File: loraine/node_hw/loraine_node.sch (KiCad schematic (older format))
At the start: 43 parts, among them CON1 BARREL_JACK, IC1 ATTINY2313A-S, P1 MOLEX, P2 MOLEX, P3 SOLDER_PAD, P4 ICSP, P5 OUTPUTS, P6 BUS, P7 BUS_THRU, Q1 BD679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

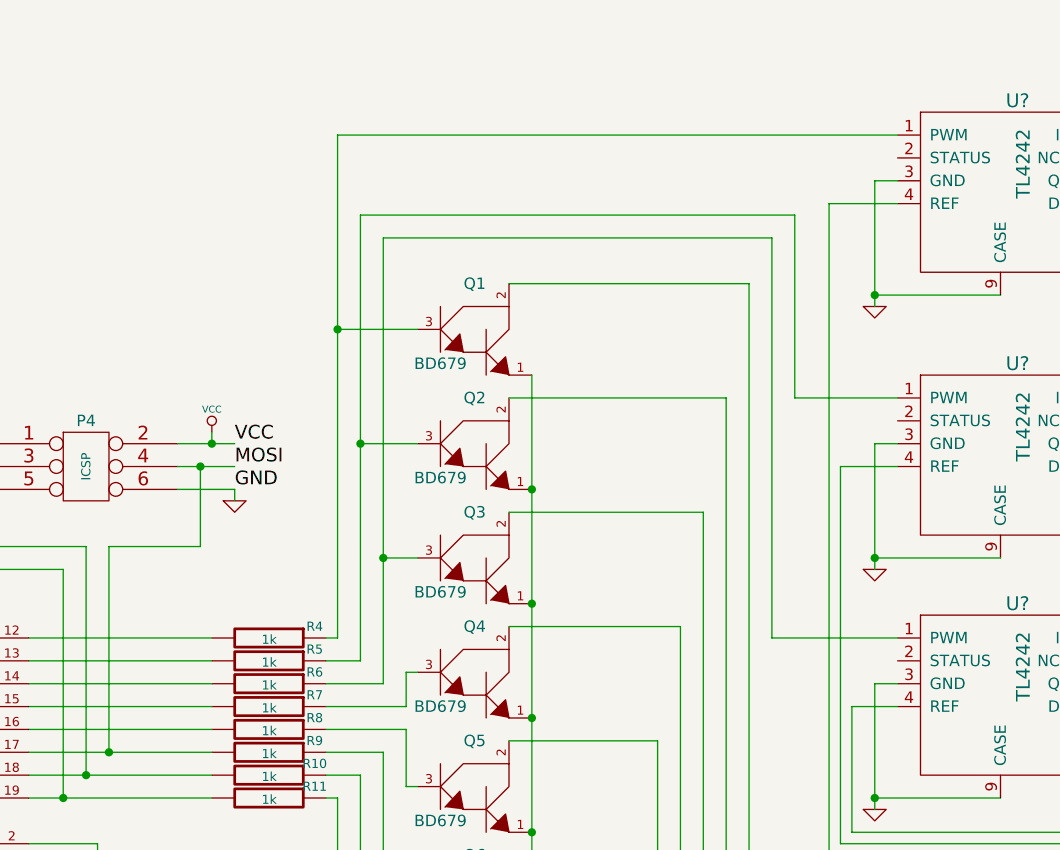
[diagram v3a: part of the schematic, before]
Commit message: Moved driver PWM conns to before BJT base resistors.
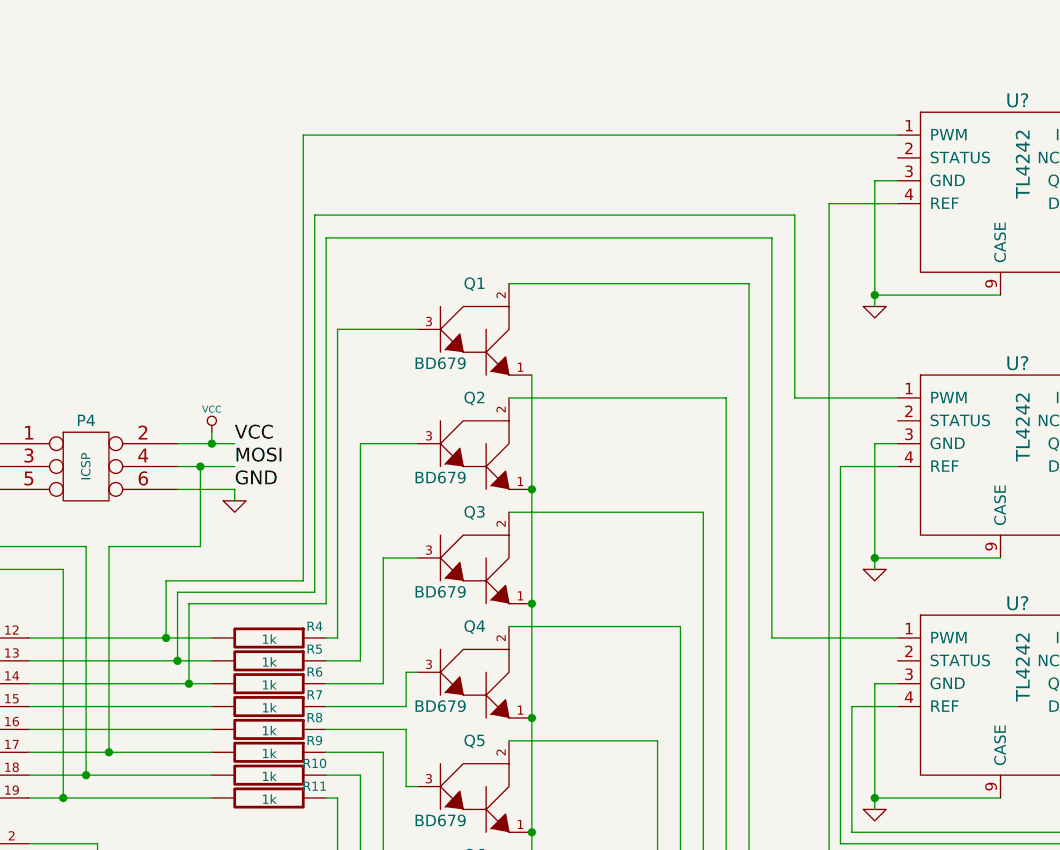
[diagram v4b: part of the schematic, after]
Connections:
- net at IC1.12 ((PCINT0/AIN0)PB0), R4.2: now also U?.1 (PWM)
- net at IC1.13 ((PCINT1/AIN1)PB1), R5.2: now also U?.1 (PWM)
- net at IC1.14 ((PCINT2/OC0A)PB2), R6.2: now also U?.1 (PWM)
- net at Q1.3, R4.1: no longer U?.1 (PWM)
- net at Q2.3, R5.1: no longer U?.1 (PWM)
- net at Q3.3, R6.1: no longer U?.1 (PWM)
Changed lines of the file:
@@
 	6150 3650 6100 3650
 Wire Wire Line
-	6150 1450 6150 3650
-Wire Wire Line
 	6250 3750 6100 3750
 Wire Wire Line
-	6250 1800 6250 3750
-Wire Wire Line
 	6250 2800 6500 2800
 Wire Wire Line
 	6350 3850 6100 3850
-Wire Wire Line
-	6350 1900 6350 3850
 Wire Wire Line
 	6350 3300 6500 3300
@@
 Connection ~ 8500 4350
 Wire Wire Line
-	6350 1900 8050 1900
+	6100 1900 8050 1900
 Wire Wire Line
 	8050 1900 8050 3650
 Wire Wire Line
 	8050 3650 8600 3650
-Connection ~ 6350 3300
-Wire Wire Line
-	6250 1800 8150 1800
+Wire Wire Line
+	6050 1800 8150 1800
 Wire Wire Line
 	8150 1800 8150 2600
 Wire Wire Line
 	8150 2600 8600 2600
-Connection ~ 6250 2800
-Wire Wire Line
-	6150 1450 8600 1450
-Connection ~ 6150 2300
+Wire Wire Line
+	6000 1450 8600 1450
 $Comp
 L R R?
@@
 Wire Wire Line
 	9600 3650 9600 3500
+Wire Wire Line
+	6150 2300 6150 3650
+Wire Wire Line
+	6250 2800 6250 3750
+Wire Wire Line
+	6350 3300 6350 3850
+Wire Wire Line
+	5500 3850 5500 3500
+Wire Wire Line
+	5500 3500 6100 3500
+Wire Wire Line
+	6100 3500 6100 1900
+Connection ~ 5500 3850
+Wire Wire Line
+	5450 3750 5450 3450
+Wire Wire Line
+	5450 3450 6050 3450
+Wire Wire Line
+	6050 3450 6050 1800
+Connection ~ 5450 3750
+Wire Wire Line
+	5400 3650 5400 3400
+Wire Wire Line
+	5400 3400 6000 3400
+Wire Wire Line
+	6000 3400 6000 1450
+Connection ~ 5400 3650
 $EndSCHEMATC

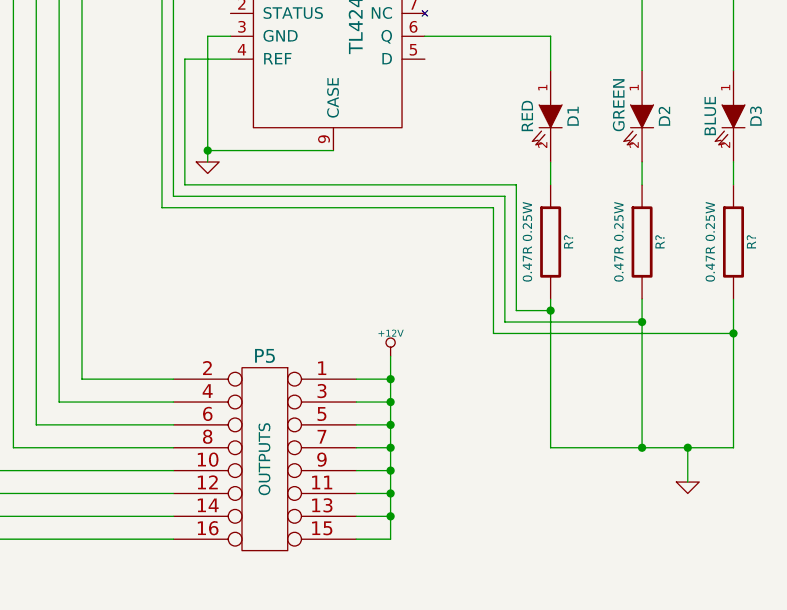
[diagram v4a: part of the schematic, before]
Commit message: Fixed driver current sense lines
TL4242 current sense lines went to ground instead of top of current sense resistors.
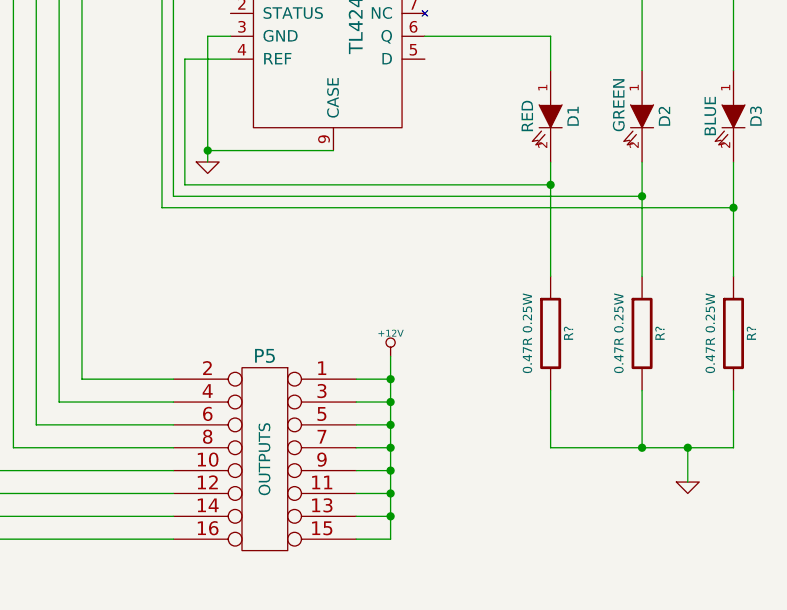
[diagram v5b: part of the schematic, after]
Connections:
- net GND: no longer U?.4 (REF), U?.4 (REF), U?.4 (REF)
- net at D1.2 (K), R?.1: now also U?.4 (REF)
- net at D2.2 (K), R?.1: now also U?.4 (REF)
- net at D3.2 (K), R?.1: now also U?.4 (REF)
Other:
- moved on the sheet: R?
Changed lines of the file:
@@
 $EndComp
-Wire Wire Line
-	10000 5000 10000 5650
 Wire Wire Line
 	10000 5650 10800 5650
-Wire Wire Line
-	10800 5650 10800 5000
-Wire Wire Line
-	10400 5000 10400 5650
 Connection ~ 10400 5650
 Wire Wire Line
@@
 L R R?
 U 1 1 5339FA1A
-P 10000 4750
-F 0 "R?" V 10080 4750 40  0000 C CNN
-F 1 "0.47R 0.25W" V 9900 4750 40  0000 C CNN
-F 2 "" V 9930 4750 30  0000 C CNN
-F 3 "" H 10000 4750 30  0000 C CNN
-	1    10000 4750
+P 10000 5150
+F 0 "R?" V 10080 5150 40  0000 C CNN
+F 1 "0.47R 0.25W" V 9900 5150 40  0000 C CNN
+F 2 "" V 9930 5150 30  0000 C CNN
+F 3 "" H 10000 5150 30  0000 C CNN
+	1    10000 5150
 	1    0    0    -1
 $EndComp
@@
 L R R?
 U 1 1 5339FA2E
-P 10400 4750
-F 0 "R?" V 10480 4750 40  0000 C CNN
-F 1 "0.47R 0.25W" V 10300 4750 40  0000 C CNN
-F 2 "" V 10330 4750 30  0000 C CNN
-F 3 "" H 10400 4750 30  0000 C CNN
-	1    10400 4750
+P 10400 5150
+F 0 "R?" V 10480 5150 40  0000 C CNN
+F 1 "0.47R 0.25W" V 10300 5150 40  0000 C CNN
+F 2 "" V 10330 5150 30  0000 C CNN
+F 3 "" H 10400 5150 30  0000 C CNN
+	1    10400 5150
 	1    0    0    -1
 $EndComp
@@
 L R R?
 U 1 1 5339FA42
-P 10800 4750
-F 0 "R?" V 10880 4750 40  0000 C CNN
-F 1 "0.47R 0.25W" V 10700 4750 40  0000 C CNN
-F 2 "" V 10730 4750 30  0000 C CNN
-F 3 "" H 10800 4750 30  0000 C CNN
-	1    10800 4750
-	1    0    0    -1
-$EndComp
-Wire Wire Line
-	10800 4500 10800 4400
-Wire Wire Line
-	10400 4400 10400 4500
-Wire Wire Line
-	10000 4500 10000 4400
+P 10800 5150
+F 0 "R?" V 10880 5150 40  0000 C CNN
+F 1 "0.47R 0.25W" V 10700 5150 40  0000 C CNN
+F 2 "" V 10730 5150 30  0000 C CNN
+F 3 "" H 10800 5150 30  0000 C CNN
+	1    10800 5150
+	1    0    0    -1
+$EndComp
 Wire Wire Line
 	10000 3850 10000 4000
@@
 	8400 3950 8400 4500
 Wire Wire Line
-	8400 4500 9850 4500
-Wire Wire Line
-	9850 4500 9850 5050
-Wire Wire Line
-	9850 5050 10000 5050
-Connection ~ 10000 5050
+	8400 4500 10000 4500
 Wire Wire Line
 	8600 2900 8350 2900
@@
 	8350 2900 8350 4550
 Wire Wire Line
-	8350 4550 9800 4550
-Wire Wire Line
-	9800 4550 9800 5100
-Wire Wire Line
-	9800 5100 10400 5100
-Connection ~ 10400 5100
+	8350 4550 10400 4550
 Wire Wire Line
 	8600 1750 8300 1750
@@
 	8300 1750 8300 4600
 Wire Wire Line
-	8300 4600 9750 4600
-Wire Wire Line
-	9750 4600 9750 5150
-Wire Wire Line
-	9750 5150 10800 5150
-Connection ~ 10800 5150
+	8300 4600 10800 4600
 Wire Wire Line
 	6900 5600 7250 5600
@@
 	6000 3400 6000 1450
 Connection ~ 5400 3650
+Connection ~ 10400 4550
+Connection ~ 10000 4500
+Connection ~ 10800 4600
+Wire Wire Line
+	10000 4400 10000 4900
+Wire Wire Line
+	10400 4400 10400 4900
+Wire Wire Line
+	10800 4400 10800 4900
+Wire Wire Line
+	10000 5400 10000 5650
+Wire Wire Line
+	10400 5400 10400 5650
+Wire Wire Line
+	10800 5650 10800 5400
 $EndSCHEMATC

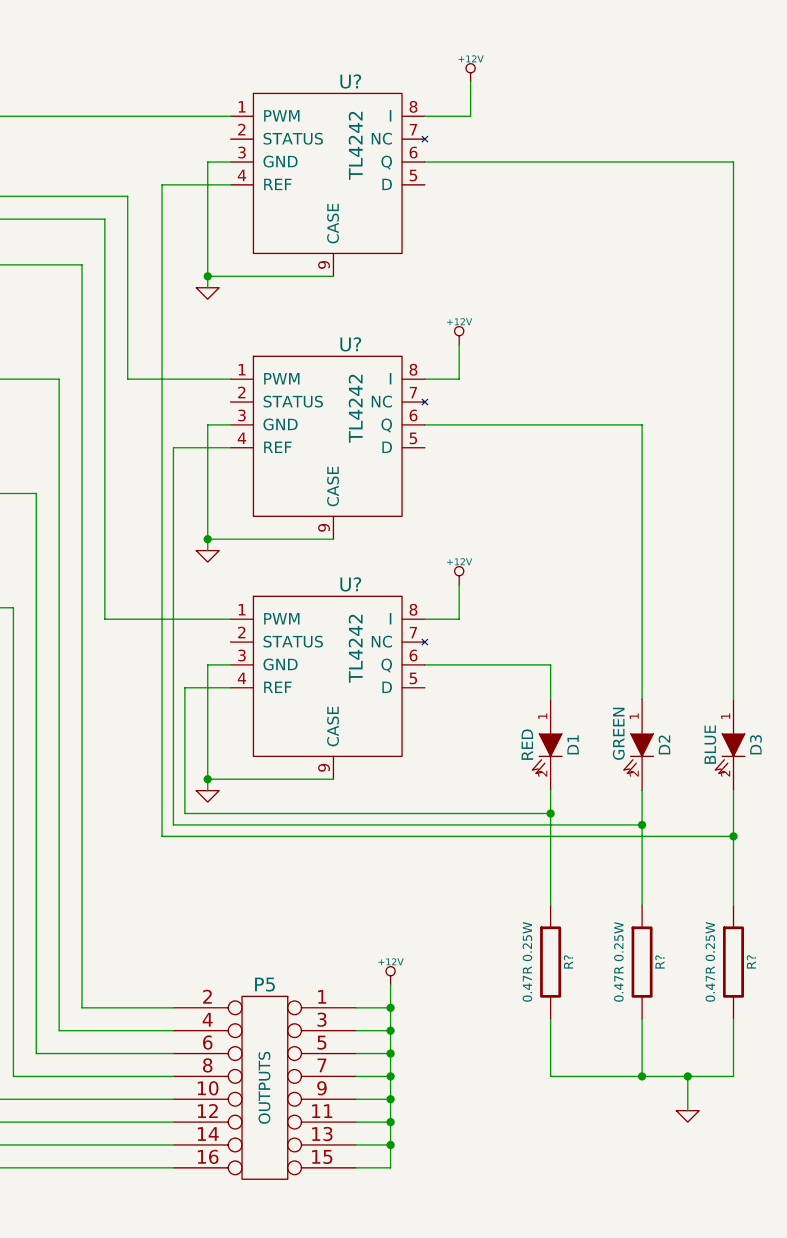
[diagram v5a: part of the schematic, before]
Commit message: Added star_led schematic component
Made new library star_led.lib with schematic component for RGB star LED with pinout matching Farnell 1716741.  Footprint to follow.
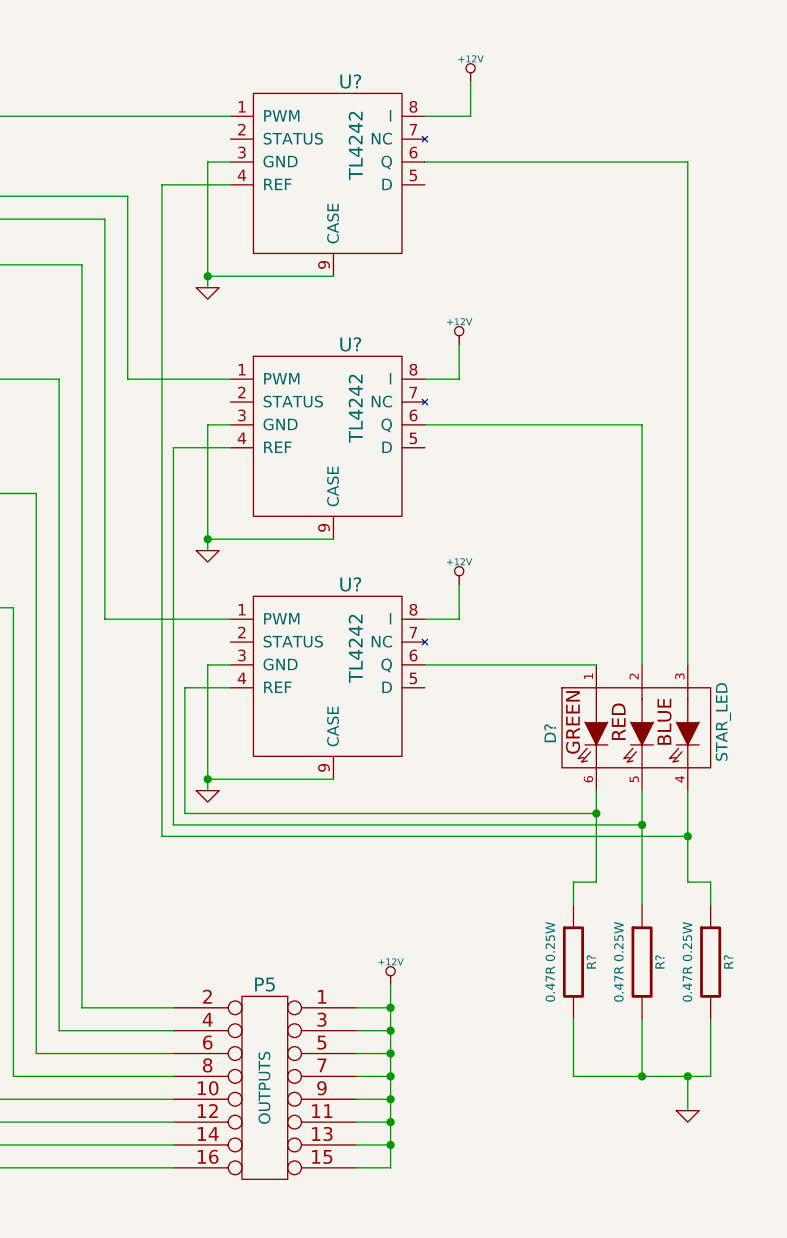
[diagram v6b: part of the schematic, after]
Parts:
- removed D1: RED, symbol LED
- removed D2: GREEN, symbol LED
- removed D3: BLUE, symbol LED
- added D?: STAR_LED, symbol STAR_LED
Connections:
- net at U?.6 (Q): now also D?.1 (G+)
- net at R?.1, U?.4 (REF): now also D?.6 (G-)
- net at U?.6 (Q): now also D?.2 (R+)
- net at R?.1, U?.4 (REF): now also D?.5 (R-)
- net at U?.6 (Q): now also D?.3 (B+)
- net at R?.1, U?.4 (REF): now also D?.4 (B-)
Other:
- moved on the sheet: R?
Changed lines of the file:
@@
 LIBS:bd679
 LIBS:tl4242
+LIBS:star_led
 LIBS:loraine_node-cache
 EELAYER 24 0
@@
 $EndComp
 $Comp
-L LED D1
-U 1 1 53389F99
-P 10000 4200
-F 0 "D1" H 10000 4300 50  0000 C CNN
-F 1 "RED" H 10000 4100 50  0000 C CNN
-F 2 "" H 10000 4200 60  0000 C CNN
-F 3 "" H 10000 4200 60  0000 C CNN
-	1    10000 4200
-	0    1    1    0
-$EndComp
-$Comp
-L LED D2
-U 1 1 53389FAD
-P 10400 4200
-F 0 "D2" H 10400 4300 50  0000 C CNN
-F 1 "GREEN" H 10350 4100 50  0000 C CNN
-F 2 "" H 10400 4200 60  0000 C CNN
-F 3 "" H 10400 4200 60  0000 C CNN
-	1    10400 4200
-	0    1    1    0
-$EndComp
-$Comp
-L LED D3
-U 1 1 53389FC1
-P 10800 4200
-F 0 "D3" H 10800 4300 50  0000 C CNN
-F 1 "BLUE" H 10800 4100 50  0000 C CNN
-F 2 "" H 10800 4200 60  0000 C CNN
-F 3 "" H 10800 4200 60  0000 C CNN
-	1    10800 4200
-	0    1    1    0
-$EndComp
-$Comp
 L C C6
 U 1 1 5338A896
@@
 	1    0    0    -1
 $EndComp
-Wire Wire Line
-	10000 5650 10800 5650
 Connection ~ 10400 5650
 Wire Wire Line
@@
 Connection ~ 10600 5650
 Wire Wire Line
-	9450 3850 10000 3850
+	9450 3850 10200 3850
 Wire Wire Line
 	9450 2800 10400 2800
-Wire Wire Line
-	9450 1650 10800 1650
 $Comp
 L +12V #PWR?
@@
 L R R?
 U 1 1 5339FA1A
-P 10000 5150
-F 0 "R?" V 10080 5150 40  0000 C CNN
-F 1 "0.47R 0.25W" V 9900 5150 40  0000 C CNN
-F 2 "" V 9930 5150 30  0000 C CNN
-F 3 "" H 10000 5150 30  0000 C CNN
-	1    10000 5150
+P 10100 5150
+F 0 "R?" V 10180 5150 40  0000 C CNN
+F 1 "0.47R 0.25W" V 10000 5150 40  0000 C CNN
+F 2 "" V 10030 5150 30  0000 C CNN
+F 3 "" H 10100 5150 30  0000 C CNN
+	1    10100 5150
 	1    0    0    -1
 $EndComp
@@
 L R R?
 U 1 1 5339FA42
-P 10800 5150
-F 0 "R?" V 10880 5150 40  0000 C CNN
-F 1 "0.47R 0.25W" V 10700 5150 40  0000 C CNN
-F 2 "" V 10730 5150 30  0000 C CNN
-F 3 "" H 10800 5150 30  0000 C CNN
-	1    10800 5150
-	1    0    0    -1
-$EndComp
-Wire Wire Line
-	10000 3850 10000 4000
-Wire Wire Line
-	10400 2800 10400 4000
-Wire Wire Line
-	10800 1650 10800 4000
+P 10700 5150
+F 0 "R?" V 10780 5150 40  0000 C CNN
+F 1 "0.47R 0.25W" V 10600 5150 40  0000 C CNN
+F 2 "" V 10630 5150 30  0000 C CNN
+F 3 "" H 10700 5150 30  0000 C CNN
+	1    10700 5150
+	1    0    0    -1
+$EndComp
 Wire Wire Line
 	8600 3950 8400 3950
@@
 	8400 3950 8400 4500
 Wire Wire Line
-	8400 4500 10000 4500
+	8400 4500 10200 4500
 Wire Wire Line
 	8600 2900 8350 2900
@@
 Wire Wire Line
 	8300 1750 8300 4600
-Wire Wire Line
-	8300 4600 10800 4600
 Wire Wire Line
 	6900 5600 7250 5600
@@
 Connection ~ 5400 3650
 Connection ~ 10400 4550
-Connection ~ 10000 4500
-Connection ~ 10800 4600
-Wire Wire Line
-	10000 4400 10000 4900
 Wire Wire Line
 	10400 4400 10400 4900
 Wire Wire Line
-	10800 4400 10800 4900
-Wire Wire Line
-	10000 5400 10000 5650
-Wire Wire Line
 	10400 5400 10400 5650
-Wire Wire Line
-	10800 5650 10800 5400
+$Comp
+L STAR_LED D?
+U 1 1 53619F29
+P 10400 4150
+F 0 "D?" V 10000 4150 50  0000 C CNN
+F 1 "STAR_LED" V 10750 4200 50  0000 C CNN
+F 2 "" V 10200 4050 60  0000 C CNN
+F 3 "" V 10200 4050 60  0000 C CNN
+	1    10400 4150
+	1    0    0    -1
+$EndComp
+Wire Wire Line
+	10200 4400 10200 4800
+Connection ~ 10200 4500
+Wire Wire Line
+	8300 4600 10600 4600
+Wire Wire Line
+	10600 4400 10600 4800
+Connection ~ 10600 4600
+Wire Wire Line
+	10400 2800 10400 3850
+Wire Wire Line
+	10600 1650 10600 3850
+Wire Wire Line
+	9450 1650 10600 1650
+Wire Wire Line
+	10100 5400 10100 5650
+Wire Wire Line
+	10100 5650 10700 5650
+Wire Wire Line
+	10700 5650 10700 5400
+Wire Wire Line
+	10100 4900 10100 4800
+Wire Wire Line
+	10100 4800 10200 4800
+Wire Wire Line
+	10700 4900 10700 4800
+Wire Wire Line
+	10700 4800 10600 4800
 $EndSCHEMATC
